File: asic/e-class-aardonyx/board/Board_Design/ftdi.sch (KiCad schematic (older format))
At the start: 62 parts, among them J11 Conn_1x8, J12 Conn_1x3_M, J13 USB_B_6PIN, J15 Conn_1x3_M, J16 USB_OTG, U11 FT2232H, U14 93LC56BT-I_OT, Y2 12MHz

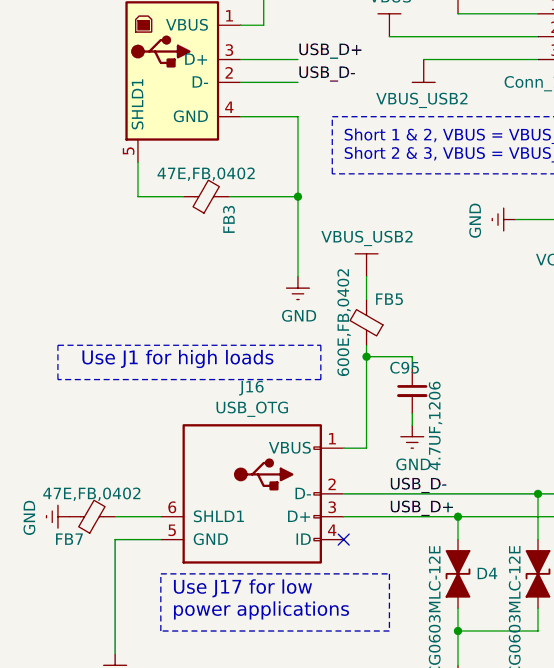
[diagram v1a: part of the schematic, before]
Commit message: updated foot print comp check
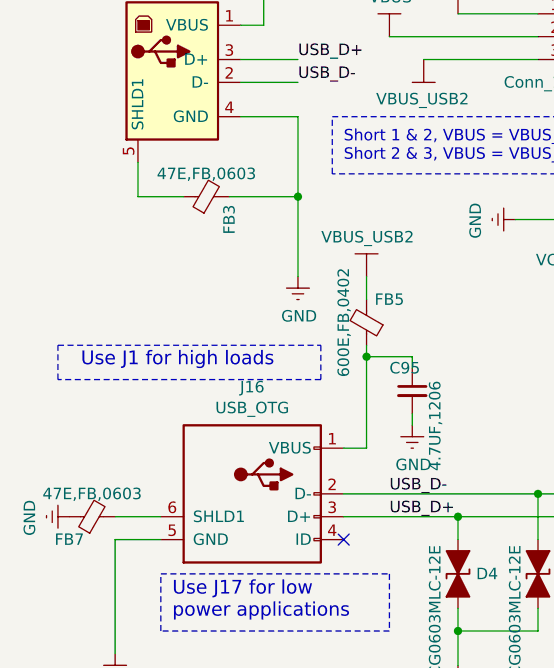
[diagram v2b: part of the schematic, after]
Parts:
- FB3, FB7: value 47E,FB,0402 -> 47E,FB,0603; footprint Inductor_SMD:L_0402_1005Metric -> Capacitor_SMD:C_0603_1608Metric
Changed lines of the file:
@@
 P 800 3750
 F 0 "FB7" V 700 3850 50  0000 C CNN
-F 1 "47E,FB,0402" V 900 3750 50  0000 C CNN
-F 2 "Inductor_SMD:L_0402_1005Metric" V 730 3750 50  0001 C CNN
+F 1 "47E,FB,0603" V 900 3750 50  0000 C CNN
+F 2 "Capacitor_SMD:C_0603_1608Metric" V 730 3750 50  0001 C CNN
 F 3 "https://www.digikey.in/product-detail/en/w%C3%BCrth-elektronik/742792608/732-1596-1-ND/1639540" H 800 3750 50  0001 C CNN
 F 4 "FERRITE BEAD 47 OHM 0603 1LN" H 800 3750 50  0001 C CNN "Description"
@@
 F 7 "Wurth Elektronik" H 800 3750 50  0001 C CNN "Maufaturer"
 	1    800  3750
-	0    -1   -1   0
-$EndComp
-$Comp
-L Aardonyx-rescue:Ferrite_Bead_Small-aardonyx FB3
-U 1 1 5EF19677
-P 1300 2350
-F 0 "FB3" H 1200 2250 50  0000 C CNN
-F 1 "47E,FB,0402" V 1400 2350 50  0000 C CNN
-F 2 "Inductor_SMD:L_0402_1005Metric" V 1230 2350 50  0001 C CNN
-F 3 "https://www.digikey.in/product-detail/en/w%C3%BCrth-elektronik/742792608/732-1596-1-ND/1639540" H 1300 2350 50  0001 C CNN
-F 4 "FERRITE BEAD 47 OHM 0603 1LN" H 1300 2350 50  0001 C CNN "Description"
-F 5 "732-1596-1-ND" H 1300 2350 50  0001 C CNN "Digikey PartNumber"
-F 6 "742792608" H 1300 2350 50  0001 C CNN "Manufactured Part Number"
-F 7 "Wurth Elektronik" H 1300 2350 50  0001 C CNN "Maufaturer"
-	1    1300 2350
 	0    -1   -1   0
 $EndComp
@@
 Wire Wire Line
 	1000 2350 1200 2350
+$Comp
+L Aardonyx-rescue:Ferrite_Bead_Small-aardonyx FB3
+U 1 1 5EF19677
+P 1300 2350
+F 0 "FB3" H 1200 2250 50  0000 C CNN
+F 1 "47E,FB,0603" V 1400 2350 50  0000 C CNN
+F 2 "Capacitor_SMD:C_0603_1608Metric" V 1230 2350 50  0001 C CNN
+F 3 "https://www.digikey.in/product-detail/en/w%C3%BCrth-elektronik/742792608/732-1596-1-ND/1639540" H 1300 2350 50  0001 C CNN
+F 4 "FERRITE BEAD 47 OHM 0603 1LN" H 1300 2350 50  0001 C CNN "Description"
+F 5 "732-1596-1-ND" H 1300 2350 50  0001 C CNN "Digikey PartNumber"
+F 6 "742792608" H 1300 2350 50  0001 C CNN "Manufactured Part Number"
+F 7 "Wurth Elektronik" H 1300 2350 50  0001 C CNN "Maufaturer"
+	1    1300 2350
+	0    -1   -1   0
+$EndComp
 $EndSCHEMATC
